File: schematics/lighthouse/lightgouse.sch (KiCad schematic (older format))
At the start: 4 parts

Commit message: lighthouse scheme
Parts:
- added D1, D2: LED, LEDs:LED-5MM, symbol LED
- added P1: 3V3, Pin_Headers:Pin_Header_Straight_1x01, symbol CONN_01X01
- added P2: GND, Pin_Headers:Pin_Header_Straight_1x01, symbol CONN_01X01
- added R1, R2: 1k, Resistors_ThroughHole:Resistor_Horizontal_RM7mm, symbol R
- added R5: 10k, w_pth_resistors:RC05, symbol R
- R3: renamed from 10k; value R -> 10K; footprint (none) -> w_pth_resistors:RC05
- R4: renamed from 10k; value R -> 10k; footprint (none) -> w_pth_resistors:RC05
- U1: renamed from U?; footprint (none) -> bugs:ESP201
- U2: renamed from U?; footprint (none) -> bugs:RC522
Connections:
- net labels removed: +3V3, GND
- wire segments 31 -> 41
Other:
- moved on the sheet: R3, R4, U2
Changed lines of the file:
@@
 EESchema Schematic File Version 2
+LIBS:lightgouse-rescue
 LIBS:power
 LIBS:device
@@
 $EndDescr
 $Comp
-L rc522 U?
+L rc522 U2
 U 1 1 5718CF80
-P 5250 2900
-F 0 "U?" H 5550 2950 60  0000 C CNN
-F 1 "rc522" H 5550 3100 60  0000 C CNN
-F 2 "" H 5150 3100 60  0000 C CNN
-F 3 "" H 5150 3100 60  0000 C CNN
-	1    5250 2900
+P 5800 2900
+F 0 "U2" H 6100 2950 60  0000 C CNN
+F 1 "rc522" H 6100 3100 60  0000 C CNN
+F 2 "bugs:RC522" H 5700 3100 60  0001 C CNN
+F 3 "" H 5700 3100 60  0000 C CNN
+	1    5800 2900
 	1    0    0    -1
 $EndComp
 $Comp
-L ESP-201 U?
+L R R4
+U 1 1 5718DD6D
+P 4000 3150
+F 0 "R4" V 3900 3150 50  0000 C CNN
+F 1 "10k" V 4000 3150 50  0000 C CNN
+F 2 "w_pth_resistors:RC05" V 3930 3150 50  0001 C CNN
+F 3 "" H 4000 3150 50  0000 C CNN
+	1    4000 3150
+	0    1    1    0
+$EndComp
+$Comp
+L R R3
+U 1 1 5718DDEA
+P 4000 2650
+F 0 "R3" V 4080 2650 50  0000 C CNN
+F 1 "10K" V 4000 2650 50  0000 C CNN
+F 2 "w_pth_resistors:RC05" V 3930 2650 50  0001 C CNN
+F 3 "" H 4000 2650 50  0000 C CNN
+	1    4000 2650
+	0    1    1    0
+$EndComp
+$Comp
+L R R5
+U 1 1 571A5ED5
+P 4000 3250
+F 0 "R5" V 4080 3250 50  0000 C CNN
+F 1 "10k" V 4000 3250 50  0000 C CNN
+F 2 "w_pth_resistors:RC05" V 3930 3250 50  0001 C CNN
+F 3 "" H 4000 3250 50  0000 C CNN
+	1    4000 3250
+	0    1    1    0
+$EndComp
+$Comp
+L CONN_01X01 P1
+U 1 1 571A6BF5
+P 3050 1350
+F 0 "P1" H 3050 1450 50  0000 C CNN
+F 1 "3V3" V 3150 1350 50  0000 C CNN
+F 2 "Pin_Headers:Pin_Header_Straight_1x01" H 3050 1350 50  0001 C CNN
+F 3 "" H 3050 1350 50  0000 C CNN
+	1    3050 1350
+	0    -1   -1   0
+$EndComp
+$Comp
+L CONN_01X01 P2
+U 1 1 571A6C6D
+P 3350 1350
+F 0 "P2" H 3350 1450 50  0000 C CNN
+F 1 "GND" V 3450 1350 50  0000 C CNN
+F 2 "Pin_Headers:Pin_Header_Straight_1x01" H 3350 1350 50  0001 C CNN
+F 3 "" H 3350 1350 50  0000 C CNN
+	1    3350 1350
+	0    -1   -1   0
+$EndComp
+$Comp
+L LED D2
+U 1 1 571A6EF4
+P 2050 3200
+F 0 "D2" H 2050 3300 50  0000 C CNN
+F 1 "LED" H 2050 3100 50  0000 C CNN
+F 2 "LEDs:LED-5MM" H 2050 3200 50  0001 C CNN
+F 3 "" H 2050 3200 50  0000 C CNN
+	1    2050 3200
+	0    1    1    0
+$EndComp
+$Comp
+L LED D1
+U 1 1 571A6FA0
+P 2150 2450
+F 0 "D1" H 2150 2550 50  0000 C CNN
+F 1 "LED" H 2150 2350 50  0000 C CNN
+F 2 "LEDs:LED-5MM" H 2150 2450 50  0001 C CNN
+F 3 "" H 2150 2450 50  0000 C CNN
+	1    2150 2450
+	0    1    1    0
+$EndComp
+$Comp
+L R R2
+U 1 1 571A710A
+P 2400 2650
+F 0 "R2" V 2480 2650 50  0000 C CNN
+F 1 "1k" V 2400 2650 50  0000 C CNN
+F 2 "Resistors_ThroughHole:Resistor_Horizontal_RM7mm" V 2330 2650 50  0001 C CNN
+F 3 "" H 2400 2650 50  0000 C CNN
+	1    2400 2650
+	0    1    1    0
+$EndComp
+$Comp
+L R R1
+U 1 1 571A724A
+P 2350 3450
+F 0 "R1" V 2430 3450 50  0000 C CNN
+F 1 "1k" V 2350 3450 50  0000 C CNN
+F 2 "Resistors_ThroughHole:Resistor_Horizontal_RM7mm" V 2280 3450 50  0001 C CNN
+F 3 "" H 2350 3450 50  0000 C CNN
+	1    2350 3450
+	0    1    1    0
+$EndComp
+$Comp
+L ESP-201 U1
 U 1 1 5718D2DA
 P 3200 3150
-F 0 "U?" H 3300 3300 60  0000 C CNN
+F 0 "U1" H 3300 3300 60  0000 C CNN
 F 1 "ESP-201" H 3200 3450 60  0000 C CNN
-F 2 "" H 3450 3350 60  0000 C CNN
+F 2 "bugs:ESP201" H 3450 3350 60  0001 C CNN
 F 3 "" H 3450 3350 60  0000 C CNN
 	1    3200 3150
@@
 	4700 2550 4700 1950
 Wire Wire Line
-	4700 1950 2200 1950
-Wire Wire Line
-	2200 1950 2200 2750
-Wire Wire Line
-	2200 2750 2600 2750
-Wire Wire Line
-	3800 2750 4700 2750
+	4700 1950 1950 1950
+Wire Wire Line
+	1950 1950 1950 2750
+Wire Wire Line
+	1950 2750 2600 2750
+Wire Wire Line
+	3800 2750 5250 2750
 Wire Wire Line
 	3800 2950 4400 2950
 Wire Wire Line
-	3800 2850 4700 2850
-Wire Wire Line
-	4700 3900 4700 3250
-Wire Wire Line
-	2600 3900 4700 3900
+	3800 2850 5250 2850
+Wire Wire Line
+	4950 3900 4950 3250
+Wire Wire Line
+	2600 3900 4950 3900
 Wire Wire Line
 	2600 3900 2600 3650
 Wire Wire Line
+	4350 3050 4350 3550
+Wire Wire Line
+	4350 3550 3800 3550
+Wire Wire Line
+	3050 1550 3050 2300
+Wire Wire Line
+	3350 1550 3350 2300
+Wire Wire Line
+	4550 3150 5250 3150
+Wire Wire Line
+	4250 2150 4250 3250
+Wire Wire Line
+	5250 2550 4700 2550
+Wire Wire Line
+	4250 3250 4150 3250
+Wire Wire Line
+	4250 3150 4150 3150
+Wire Wire Line
+	3850 3150 3800 3150
+Wire Wire Line
+	3800 3250 3850 3250
+Connection ~ 4250 3150
+Connection ~ 3050 2150
+Wire Wire Line
+	2550 2650 2600 2650
+Wire Wire Line
+	2050 2200 4150 2200
+Wire Wire Line
+	4150 2200 4150 2650
+Connection ~ 3350 2200
+Wire Wire Line
+	3850 2650 3800 2650
+Wire Wire Line
+	3050 2150 4250 2150
+Wire Wire Line
+	2050 3000 2050 2200
+Connection ~ 2150 2200
+Wire Wire Line
+	4550 3450 3800 3450
+Wire Wire Line
+	4550 3150 4550 3450
+Wire Wire Line
+	2500 3450 2600 3450
+Wire Wire Line
+	2550 3550 2600 3550
+Wire Wire Line
+	2050 3450 2200 3450
+Wire Wire Line
+	2050 3400 2050 3450
+Wire Wire Line
+	2150 2250 2150 2200
+Wire Wire Line
+	2250 2650 2150 2650
+Wire Wire Line
 	4400 2950 4400 2650
 Wire Wire Line
-	4400 2650 4700 2650
-Wire Wire Line
-	4700 3050 3950 3050
-Wire Wire Line
-	3950 3050 3950 3550
-Wire Wire Line
-	3950 3550 3800 3550
-$Comp
-L +3V3 #PWR?
-U 1 1 5718DC65
-P 3050 1650
-F 0 "#PWR?" H 3050 1500 50  0001 C CNN
-F 1 "+3V3" H 3050 1790 50  0000 C CNN
-F 2 "" H 3050 1650 50  0000 C CNN
-F 3 "" H 3050 1650 50  0000 C CNN
-	1    3050 1650
-	1    0    0    -1
-$EndComp
-Wire Wire Line
-	3050 1650 3050 2300
-$Comp
-L GND #PWR?
-U 1 1 5718DCCC
-P 3350 1650
-F 0 "#PWR?" H 3350 1400 50  0001 C CNN
-F 1 "GND" H 3350 1500 50  0000 C CNN
-F 2 "" H 3350 1650 50  0000 C CNN
-F 3 "" H 3350 1650 50  0000 C CNN
-	1    3350 1650
-	-1   0    0    1
-$EndComp
-Wire Wire Line
-	3350 1650 3350 2300
-Wire Wire Line
-	4750 3150 4200 3150
-Wire Wire Line
-	4200 3150 4200 3850
-Wire Wire Line
-	4200 3850 2500 3850
-Wire Wire Line
-	2500 3850 2500 3450
-Wire Wire Line
-	2500 3450 2600 3450
-$Comp
-L R 10k
-U 1 1 5718DD6D
-P 2850 1800
-F 0 "10k" V 2930 1800 50  0000 C CNN
-F 1 "R" V 2850 1800 50  0000 C CNN
-F 2 "" V 2780 1800 50  0000 C CNN
-F 3 "" H 2850 1800 50  0000 C CNN
-	1    2850 1800
-	0    1    1    0
-$EndComp
-Wire Wire Line
-	3000 1800 3050 1800
-Connection ~ 3050 1800
-Wire Wire Line
-	3800 3150 3900 3150
-Wire Wire Line
-	3900 3150 3900 1350
-Wire Wire Line
-	3900 1350 2650 1350
-Wire Wire Line
-	2650 1350 2650 1800
-Wire Wire Line
-	2650 1800 2700 1800
-$Comp
-L R 10k
-U 1 1 5718DDEA
-P 3550 1800
-F 0 "10k" V 3630 1800 50  0000 C CNN
-F 1 "R" V 3550 1800 50  0000 C CNN
-F 2 "" V 3480 1800 50  0000 C CNN
-F 3 "" H 3550 1800 50  0000 C CNN
-	1    3550 1800
-	0    1    1    0
-$EndComp
-Wire Wire Line
-	3400 1800 3350 1800
-Connection ~ 3350 1800
-Wire Wire Line
-	3700 1800 3800 1800
-Wire Wire Line
-	3800 1800 3800 2650
+	4400 2650 5250 2650
+Wire Wire Line
+	4350 3050 5250 3050
+Wire Wire Line
+	5250 3250 5150 3250
+Wire Wire Line
+	5150 3250 5150 1750
+Wire Wire Line
+	5150 1750 3050 1750
+Connection ~ 3050 1750
 $EndSCHEMATC

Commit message: lighthouse schematic update
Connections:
- wire segments 41 -> 37
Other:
- moved on the sheet: D2, R1
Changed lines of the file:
@@
 L LED D2
 U 1 1 571A6EF4
-P 2050 3200
-F 0 "D2" H 2050 3300 50  0000 C CNN
-F 1 "LED" H 2050 3100 50  0000 C CNN
-F 2 "LEDs:LED-5MM" H 2050 3200 50  0001 C CNN
-F 3 "" H 2050 3200 50  0000 C CNN
-	1    2050 3200
+P 1900 2500
+F 0 "D2" H 1900 2600 50  0000 C CNN
+F 1 "LED" H 1900 2400 50  0000 C CNN
+F 2 "LEDs:LED-5MM" H 1900 2500 50  0001 C CNN
+F 3 "" H 1900 2500 50  0000 C CNN
+	1    1900 2500
 	0    1    1    0
 $EndComp
@@
 U 1 1 571A710A
 P 2400 2650
-F 0 "R2" V 2480 2650 50  0000 C CNN
+F 0 "R2" V 2300 2650 50  0000 C CNN
 F 1 "1k" V 2400 2650 50  0000 C CNN
 F 2 "Resistors_ThroughHole:Resistor_Horizontal_RM7mm" V 2330 2650 50  0001 C CNN
@@
 L R R1
 U 1 1 571A724A
-P 2350 3450
-F 0 "R1" V 2430 3450 50  0000 C CNN
-F 1 "1k" V 2350 3450 50  0000 C CNN
-F 2 "Resistors_ThroughHole:Resistor_Horizontal_RM7mm" V 2280 3450 50  0001 C CNN
-F 3 "" H 2350 3450 50  0000 C CNN
-	1    2350 3450
+P 2400 2750
+F 0 "R1" V 2480 2750 50  0000 C CNN
+F 1 "1k" V 2400 2750 50  0000 C CNN
+F 2 "Resistors_ThroughHole:Resistor_Horizontal_RM7mm" V 2330 2750 50  0001 C CNN
+F 3 "" H 2400 2750 50  0000 C CNN
+	1    2400 2750
 	0    1    1    0
 $EndComp
@@
 $EndComp
 Wire Wire Line
-	4700 2550 4700 1950
+	4700 1950 4700 2550
 Wire Wire Line
-	4700 1950 1950 1950
-Wire Wire Line
-	1950 1950 1950 2750
-Wire Wire Line
-	1950 2750 2600 2750
+	1700 1950 4700 1950
 Wire Wire Line
 	3800 2750 5250 2750
@@
 Wire Wire Line
 	3800 2850 5250 2850
-Wire Wire Line
-	4950 3900 4950 3250
-Wire Wire Line
-	2600 3900 4950 3900
-Wire Wire Line
-	2600 3900 2600 3650
 Wire Wire Line
 	4350 3050 4350 3550
@@
 	4250 2150 4250 3250
 Wire Wire Line
-	5250 2550 4700 2550
+	4700 2550 5250 2550
 Wire Wire Line
 	4250 3250 4150 3250
@@
 	2550 2650 2600 2650
 Wire Wire Line
-	2050 2200 4150 2200
+	1900 2200 4150 2200
 Wire Wire Line
 	4150 2200 4150 2650
@@
 Wire Wire Line
 	3050 2150 4250 2150
-Wire Wire Line
-	2050 3000 2050 2200
 Connection ~ 2150 2200
 Wire Wire Line
@@
 Wire Wire Line
 	4550 3150 4550 3450
-Wire Wire Line
-	2500 3450 2600 3450
-Wire Wire Line
-	2550 3550 2600 3550
-Wire Wire Line
-	2050 3450 2200 3450
-Wire Wire Line
-	2050 3400 2050 3450
 Wire Wire Line
 	2150 2250 2150 2200
@@
 	5150 1750 3050 1750
 Connection ~ 3050 1750
+Wire Wire Line
+	2550 2750 2600 2750
+Wire Wire Line
+	1900 2700 1900 2750
+Wire Wire Line
+	1900 2750 2250 2750
+Wire Wire Line
+	1900 2300 1900 2200
+Wire Wire Line
+	1700 1950 1700 3450
+Wire Wire Line
+	1700 3450 2600 3450
 $EndSCHEMATC

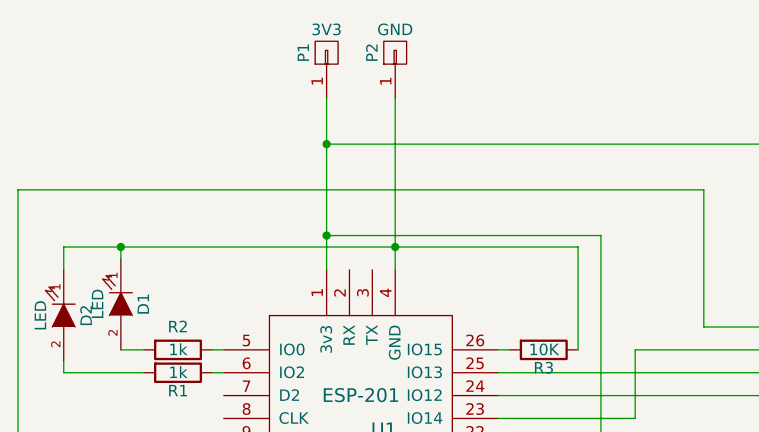
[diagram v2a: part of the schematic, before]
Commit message: Update schematics for whiskers
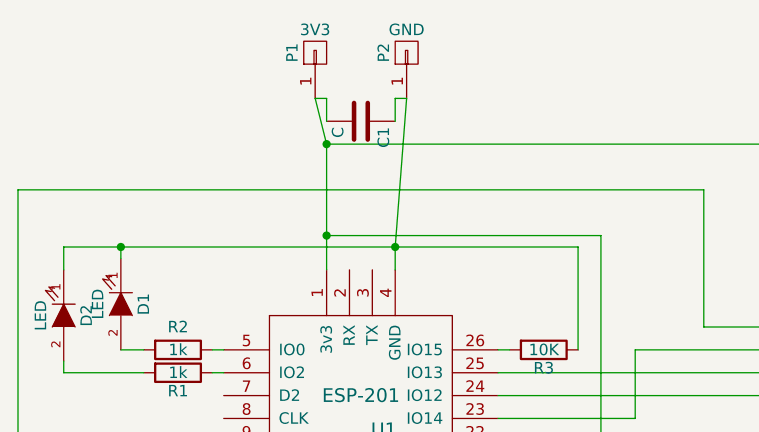
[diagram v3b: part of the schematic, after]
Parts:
- added C1: C, Capacitors_ThroughHole:C_Disc_D3_P2.5, symbol C
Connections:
- net at P1.1 (P1), R4.1, R5.1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: now also C1.2
- net at D1.1 (K), D2.1 (K), P2.1 (P1)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: now also C1.1
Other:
- moved on the sheet: P1, P2
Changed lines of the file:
@@
 L CONN_01X01 P1
 U 1 1 571A6BF5
-P 3050 1350
-F 0 "P1" H 3050 1450 50  0000 C CNN
-F 1 "3V3" V 3150 1350 50  0000 C CNN
-F 2 "Pin_Headers:Pin_Header_Straight_1x01" H 3050 1350 50  0001 C CNN
-F 3 "" H 3050 1350 50  0000 C CNN
-	1    3050 1350
+P 3000 1350
+F 0 "P1" H 3000 1450 50  0000 C CNN
+F 1 "3V3" V 3100 1350 50  0000 C CNN
+F 2 "Pin_Headers:Pin_Header_Straight_1x01" H 3000 1350 50  0001 C CNN
+F 3 "" H 3000 1350 50  0000 C CNN
+	1    3000 1350
 	0    -1   -1   0
 $EndComp
@@
 L CONN_01X01 P2
 U 1 1 571A6C6D
-P 3350 1350
-F 0 "P2" H 3350 1450 50  0000 C CNN
-F 1 "GND" V 3450 1350 50  0000 C CNN
-F 2 "Pin_Headers:Pin_Header_Straight_1x01" H 3350 1350 50  0001 C CNN
-F 3 "" H 3350 1350 50  0000 C CNN
-	1    3350 1350
+P 3400 1350
+F 0 "P2" H 3400 1450 50  0000 C CNN
+F 1 "GND" V 3500 1350 50  0000 C CNN
+F 2 "Pin_Headers:Pin_Header_Straight_1x01" H 3400 1350 50  0001 C CNN
+F 3 "" H 3400 1350 50  0000 C CNN
+	1    3400 1350
 	0    -1   -1   0
 $EndComp
@@
 	4350 3550 3800 3550
 Wire Wire Line
-	3050 1550 3050 2300
+	3000 1550 3050 1750
 Wire Wire Line
-	3350 1550 3350 2300
+	3050 1750 3050 2300
+Wire Wire Line
+	3350 2200 3400 1550
+Wire Wire Line
+	3350 2200 3350 2300
 Wire Wire Line
 	4550 3150 5250 3150
@@
 Wire Wire Line
 	1700 3450 2600 3450
+$Comp
+L C C1
+U 1 1 57248AF2
+P 3200 1650
+F 0 "C1" H 3225 1750 50  0000 L CNN
+F 1 "C" H 3225 1550 50  0000 L CNN
+F 2 "Capacitors_ThroughHole:C_Disc_D3_P2.5" H 3238 1500 50  0001 C CNN
+F 3 "" H 3200 1650 50  0000 C CNN
+	1    3200 1650
+	0    1    1    0
+$EndComp
+Wire Wire Line
+	3050 1650 3050 1550
+Wire Wire Line
+	3050 1550 3000 1550
+Wire Wire Line
+	3350 1650 3350 1550
+Wire Wire Line
+	3350 1550 3400 1550
 $EndSCHEMATC

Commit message: SCHEMATICS: prepare Lighthouse for production
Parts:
- removed C1: C, Capacitors_ThroughHole:C_Disc_D3_P2.5, symbol C
- added C2: 100mkF, bugs:capasitor, symbol CP
- added C3: 1000mkF, bugs:capasitor, symbol CP
- added D3: D_Schottky, Diodes_ThroughHole:Diode_DO-41_SOD81_Horizontal_RM10, symbol D_Schottky
- added L1: 100mkH, Discret:CP4, symbol L_Small
- added P3: TX, Pin_Headers:Pin_Header_Straight_1x01, symbol CONN_01X01
- added P4: RX, Pin_Headers:Pin_Header_Straight_1x01, symbol CONN_01X01
- added U3: LM2576, TO_SOT_Packages_THT:Pentawatt_Neutral_Straight_Vertical_TO220-5-T05A, symbol LM2576
- P1: value 3V3 -> VCC
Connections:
- net at R4.1, R5.1, U1.1 (3v3)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: now also C3.1, L1.2, U3.~ (FEEDBACK); no longer P1.1 (P1)
- net at U1.2 (RX): now also P4.1 (P1)
- net at U1.3 (TX): now also P3.1 (P1)
- net at D1.1 (K), D2.1 (K), P2.1 (P1)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: now also C2.2, C3.2, D3.2 (A), U3.2 (GND), U3.3 (ON/OFF)
- new net: C2.1, P1.1 (P1), U3.1 (VIN)
- new net: D3.1 (K), L1.1, U3.4 (VOUT)
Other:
- moved on the sheet: D1, D2, P1, P2, R1, R2, R3, R4, R5, U1, U2
